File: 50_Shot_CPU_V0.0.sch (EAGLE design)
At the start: 74 parts, among them IC1 PIC24FJ128GA010, J1 J12, J10 22-23-2021, J11 22-23-2061, J12 A311422_nd, J13 22-23-2021, J14 22-23-2021, J2 J2, J3 22-23-2021, J4 22-23-2021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

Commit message: testing push/pull
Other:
- note added: "Adding this text, pushing, deleting from laptop, pulling"
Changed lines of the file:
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@@
 <?xml version="1.0" encoding="utf-8"?>
 <!DOCTYPE eagle SYSTEM "eagle.dtd">
-<eagle version="7.6.0">
+<eagle version="7.7.0">
 <drawing>
 <settings>
@@
 <frame x1="-182.88" y1="-76.2" x2="276.86" y2="220.98" columns="8" rows="5" layer="91"/>
 <text x="-129.54" y="-38.1" size="1.778" layer="91">***Note: Change R9 to 000 ohm if used for -X of touch screen. </text>
+<text x="132.08" y="167.64" size="1.778" layer="91">Adding this text, pushing, deleting from laptop, pulling</text>
 </plain>
 <instances>

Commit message: trying this again
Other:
- note added: "it worked, try yhis again"
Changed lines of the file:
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@@
 <text x="-129.54" y="-38.1" size="1.778" layer="91">***Note: Change R9 to 000 ohm if used for -X of touch screen. </text>
 <text x="132.08" y="167.64" size="1.778" layer="91">Adding this text, pushing, deleting from laptop, pulling</text>
+<text x="144.78" y="162.56" size="1.778" layer="91">it worked, try yhis again</text>
 </plain>
 <instances>

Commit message: add relay board
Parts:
- removed X4: 22-23-2111, con-molex:22-23-2111
- added R19: 1k, rcl-2:R-US_M0805
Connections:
- removed net RF3: IC1.U1TX/RF3, J11-1.S
- new net ###: J11-1.S
- new net SHIFT_EN: IC1.U1TX/RF3, R19.1, X5-7.S
- net +12V: now also C8.1, J1-4.S, X5-1.S
- net ARM_RELAY: no longer X5-7.S
- net VCC: no longer J1-4.S
- net VDD: now also R19.2; no longer C8.1, X5-1.S
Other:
- note removed: "Dummy Header"
- moved on the sheet: C17
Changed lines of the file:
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@@
 <part name="J14" library="Mine" deviceset="22-23-2021" device=""/>
 <part name="X5" library="con-molex" deviceset="22-23-2111" device=""/>
-<part name="X4" library="con-molex" deviceset="22-23-2111" device=""/>
 <part name="X3" library="con-molex" deviceset="22-23-2081" device=""/>
 <part name="C7" library="rcl" deviceset="C-US" device="C0805" value="0.01uF"/>
@@
 <part name="C23" library="Mine" deviceset="CAP3X3" device="" value="10uF"/>
 <part name="R18" library="rcl" deviceset="R-US_" device="M0805" value="1k"/>
+<part name="R19" library="rcl-2" deviceset="R-US_" device="M0805" value="1k"/>
 </parts>
 <sheets>
@@
 <text x="-22.86" y="86.36" size="1.778" layer="91">Circuit Board Header</text>
 <text x="-43.18" y="200.66" size="1.778" layer="91">I2C Header</text>
-<text x="-15.24" y="38.1" size="1.778" layer="91">Dummy Header</text>
 <text x="-142.24" y="152.4" size="1.778" layer="91">S/M Switch</text>
 <text x="-144.78" y="109.22" size="1.778" layer="91">Fire Switch</text>
@@
 <attribute name="VALUE" x="227.584" y="37.211" size="1.778" layer="96" rot="R180"/>
 </instance>
-<instance part="C17" gate="G$1" x="154.94" y="-40.64" smashed="yes" rot="R180">
-<attribute name="NAME" x="153.924" y="-41.275" size="1.778" layer="95" rot="R180"/>
-<attribute name="VALUE" x="153.924" y="-36.449" size="1.778" layer="96" rot="R180"/>
+<instance part="C17" gate="G$1" x="160.02" y="-40.64" smashed="yes" rot="R180">
+<attribute name="NAME" x="159.004" y="-41.275" size="1.778" layer="95" rot="R180"/>
+<attribute name="VALUE" x="159.004" y="-36.449" size="1.778" layer="96" rot="R180"/>
 </instance>
 <instance part="J13" gate="-1" x="2.54" y="149.86" smashed="yes" rot="R180">
@@
 <instance part="X5" gate="-10" x="-5.08" y="48.26"/>
 <instance part="X5" gate="-11" x="-5.08" y="45.72"/>
-<instance part="X4" gate="-1" x="-12.7" y="33.02"/>
-<instance part="X4" gate="-2" x="-12.7" y="30.48"/>
-<instance part="X4" gate="-3" x="-12.7" y="27.94"/>
-<instance part="X4" gate="-4" x="-12.7" y="25.4"/>
-<instance part="X4" gate="-5" x="-12.7" y="22.86"/>
-<instance part="X4" gate="-6" x="-12.7" y="20.32"/>
-<instance part="X4" gate="-7" x="-12.7" y="17.78"/>
-<instance part="X4" gate="-8" x="-12.7" y="15.24"/>
-<instance part="X4" gate="-9" x="-12.7" y="12.7"/>
-<instance part="X4" gate="-10" x="-12.7" y="10.16"/>
-<instance part="X4" gate="-11" x="-12.7" y="7.62"/>
 <instance part="X3" gate="-1" x="-33.02" y="180.34" rot="R180"/>
 <instance part="X3" gate="-2" x="-33.02" y="182.88" rot="R180"/>
@@
 <attribute name="NAME" x="-135.128" y="130.0734" size="1.778" layer="95" rot="R180"/>
 <attribute name="VALUE" x="-124.714" y="125.73" size="1.778" layer="96" rot="R180"/>
+</instance>
+<instance part="R19" gate="G$1" x="203.2" y="-25.4" smashed="yes" rot="R90">
+<attribute name="NAME" x="201.7014" y="-29.21" size="1.778" layer="95" rot="R90"/>
+<attribute name="VALUE" x="206.502" y="-29.21" size="1.778" layer="96" rot="R90"/>
 </instance>
 </instances>
@@
 <wire x1="5.08" y1="149.86" x2="15.24" y2="149.86" width="0.1524" layer="91"/>
 </segment>
+<segment>
+<wire x1="-7.62" y1="71.12" x2="-15.24" y2="71.12" width="0.1524" layer="91"/>
+<label x="-15.24" y="71.12" size="1.778" layer="95" rot="R180" xref="yes"/>
+<pinref part="C8" gate="G$1" pin="1"/>
+<wire x1="-12.7" y1="81.28" x2="-12.7" y2="83.82" width="0.1524" layer="91"/>
+<wire x1="-12.7" y1="83.82" x2="-7.62" y2="83.82" width="0.1524" layer="91"/>
+<wire x1="-7.62" y1="83.82" x2="-7.62" y2="71.12" width="0.1524" layer="91"/>
+<pinref part="X5" gate="-1" pin="S"/>
+<junction x="-7.62" y="71.12"/>
+</segment>
+<segment>
+<pinref part="J1" gate="-4" pin="S"/>
+<wire x1="-157.48" y1="132.08" x2="-111.76" y2="132.08" width="0.1524" layer="91"/>
+<label x="-111.76" y="132.08" size="1.778" layer="95" xref="yes"/>
+</segment>
 </net>
 <net name="GND" class="0">
@@
 <junction x="15.24" y="-2.54"/>
 <junction x="15.24" y="-35.56"/>
-<wire x1="154.94" y1="-35.56" x2="147.32" y2="-35.56" width="0.1524" layer="91"/>
+<wire x1="160.02" y1="-35.56" x2="147.32" y2="-35.56" width="0.1524" layer="91"/>
 <wire x1="147.32" y1="-35.56" x2="124.46" y2="-35.56" width="0.1524" layer="91"/>
 <wire x1="124.46" y1="-35.56" x2="111.76" y2="-35.56" width="0.1524" layer="91"/>
@@
 <label x="261.62" y="127" size="1.778" layer="95" xref="yes"/>
 </segment>
-<segment>
-<pinref part="J1" gate="-4" pin="S"/>
-<wire x1="-157.48" y1="132.08" x2="-111.76" y2="132.08" width="0.1524" layer="91"/>
-<label x="-111.76" y="132.08" size="1.778" layer="95" xref="yes"/>
-</segment>
 </net>
 <net name="VDD" class="0">
@@
 <wire x1="60.96" y1="48.26" x2="27.94" y2="48.26" width="0.1524" layer="91"/>
 <junction x="27.94" y="48.26"/>
-<wire x1="27.94" y1="93.98" x2="231.14" y2="93.98" width="0.1524" layer="91"/>
+<wire x1="27.94" y1="93.98" x2="238.76" y2="93.98" width="0.1524" layer="91"/>
 <junction x="27.94" y="93.98"/>
-<wire x1="231.14" y1="93.98" x2="231.14" y2="17.78" width="0.1524" layer="91"/>
+<wire x1="238.76" y1="93.98" x2="238.76" y2="17.78" width="0.1524" layer="91"/>
 <pinref part="IC1" gate="G$1" pin="VDD@5"/>
 <pinref part="IC1" gate="G$1" pin="VDD@4"/>
-<wire x1="231.14" y1="17.78" x2="223.52" y2="17.78" width="0.1524" layer="91"/>
+<wire x1="238.76" y1="17.78" x2="223.52" y2="17.78" width="0.1524" layer="91"/>
 <wire x1="223.52" y1="17.78" x2="195.58" y2="17.78" width="0.1524" layer="91"/>
 <wire x1="149.86" y1="-17.78" x2="149.86" y2="-45.72" width="0.1524" layer="91"/>
-<wire x1="149.86" y1="-45.72" x2="154.94" y2="-45.72" width="0.1524" layer="91"/>
-<wire x1="154.94" y1="-45.72" x2="231.14" y2="-45.72" width="0.1524" layer="91"/>
-<wire x1="231.14" y1="-45.72" x2="231.14" y2="17.78" width="0.1524" layer="91"/>
-<junction x="231.14" y="17.78"/>
+<wire x1="149.86" y1="-45.72" x2="160.02" y2="-45.72" width="0.1524" layer="91"/>
+<wire x1="160.02" y1="-45.72" x2="238.76" y2="-45.72" width="0.1524" layer="91"/>
+<wire x1="238.76" y1="-45.72" x2="238.76" y2="17.78" width="0.1524" layer="91"/>
+<junction x="238.76" y="17.78"/>
 <pinref part="C11" gate="G$1" pin="1"/>
 <wire x1="22.86" y1="38.1" x2="22.86" y2="48.26" width="0.1524" layer="91"/>
@@
 <wire x1="127" y1="-45.72" x2="149.86" y2="-45.72" width="0.1524" layer="91"/>
 <pinref part="C17" gate="G$1" pin="1"/>
-<wire x1="154.94" y1="-43.18" x2="154.94" y2="-45.72" width="0.1524" layer="91"/>
-<junction x="154.94" y="-45.72"/>
+<wire x1="160.02" y1="-43.18" x2="160.02" y2="-45.72" width="0.1524" layer="91"/>
+<junction x="160.02" y="-45.72"/>
 <pinref part="IC1" gate="G$1" pin="VDD@3"/>
 <wire x1="127" y1="-17.78" x2="127" y2="-45.72" width="0.1524" layer="91"/>
@@
 </segment>
 <segment>
-<wire x1="-7.62" y1="71.12" x2="-17.78" y2="71.12" width="0.1524" layer="91"/>
-<label x="-17.78" y="71.12" size="1.778" layer="95" rot="R180" xref="yes"/>
-<pinref part="C8" gate="G$1" pin="1"/>
-<wire x1="-12.7" y1="81.28" x2="-12.7" y2="83.82" width="0.1524" layer="91"/>
-<wire x1="-12.7" y1="83.82" x2="-7.62" y2="83.82" width="0.1524" layer="91"/>
-<wire x1="-7.62" y1="83.82" x2="-7.62" y2="71.12" width="0.1524" layer="91"/>
-<pinref part="X5" gate="-1" pin="S"/>
-<junction x="-7.62" y="71.12"/>
-</segment>
-<segment>
 <pinref part="X3" gate="-8" pin="S"/>
 <label x="-17.78" y="198.12" size="1.778" layer="95" xref="yes"/>
@@
 <wire x1="58.42" y1="5.08" x2="55.88" y2="5.08" width="0.1524" layer="91"/>
 <label x="55.88" y="5.08" size="1.778" layer="95" rot="R180" xref="yes"/>
+</segment>
+<segment>
+<pinref part="R19" gate="G$1" pin="2"/>
+<wire x1="203.2" y1="-20.32" x2="203.2" y2="-17.78" width="0.1524" layer="91"/>
+<wire x1="203.2" y1="-17.78" x2="205.74" y2="-17.78" width="0.1524" layer="91"/>
+<label x="205.74" y="-17.78" size="1.778" layer="95" xref="yes"/>
 </segment>
 </net>
@@
 </segment>
 </net>
-<net name="RF3" class="0">
-<segment>
-<pinref part="IC1" gate="G$1" pin="U1TX/RF3"/>
-<wire x1="195.58" y1="-10.16" x2="198.12" y2="-10.16" width="0.1524" layer="91"/>
-<wire x1="198.12" y1="-10.16" x2="198.12" y2="-17.78" width="0.1524" layer="91"/>
-<wire x1="198.12" y1="-17.78" x2="203.2" y2="-17.78" width="0.1524" layer="91"/>
-<label x="203.2" y="-17.78" size="1.778" layer="95" xref="yes"/>
-</segment>
+<net name="###" class="0">
 <segment>
 <wire x1="-48.26" y1="7.62" x2="-33.02" y2="7.62" width="0.1524" layer="91"/>
@@
 <wire x1="-101.6" y1="144.78" x2="-111.76" y2="144.78" width="0.1524" layer="91"/>
 <label x="-111.76" y="144.78" size="1.778" layer="95" rot="R180" xref="yes"/>
-</segment>
-<segment>
-<wire x1="-7.62" y1="55.88" x2="-10.16" y2="55.88" width="0.1524" layer="91"/>
-<label x="-10.16" y="55.88" size="1.778" layer="95" rot="R180" xref="yes"/>
-<pinref part="X5" gate="-7" pin="S"/>
 </segment>
 </net>
@@
 </segment>
 </net>
+<net name="SHIFT_EN" class="0">
+<segment>
+<wire x1="-7.62" y1="55.88" x2="-10.16" y2="55.88" width="0.1524" layer="91"/>
+<label x="-10.16" y="55.88" size="1.778" layer="95" rot="R180" xref="yes"/>
+<pinref part="X5" gate="-7" pin="S"/>
+</segment>
+<segment>
+<pinref part="IC1" gate="G$1" pin="U1TX/RF3"/>
+<wire x1="195.58" y1="-10.16" x2="198.12" y2="-10.16" width="0.1524" layer="91"/>
+<wire x1="198.12" y1="-10.16" x2="198.12" y2="-33.02" width="0.1524" layer="91"/>
+<wire x1="198.12" y1="-33.02" x2="203.2" y2="-33.02" width="0.1524" layer="91"/>
+<label x="210.82" y="-33.02" size="1.778" layer="95" xref="yes"/>
+<pinref part="R19" gate="G$1" pin="1"/>
+<wire x1="203.2" y1="-33.02" x2="210.82" y2="-33.02" width="0.1524" layer="91"/>
+<wire x1="203.2" y1="-30.48" x2="203.2" y2="-33.02" width="0.1524" layer="91"/>
+<junction x="203.2" y="-33.02"/>
+</segment>
+</net>

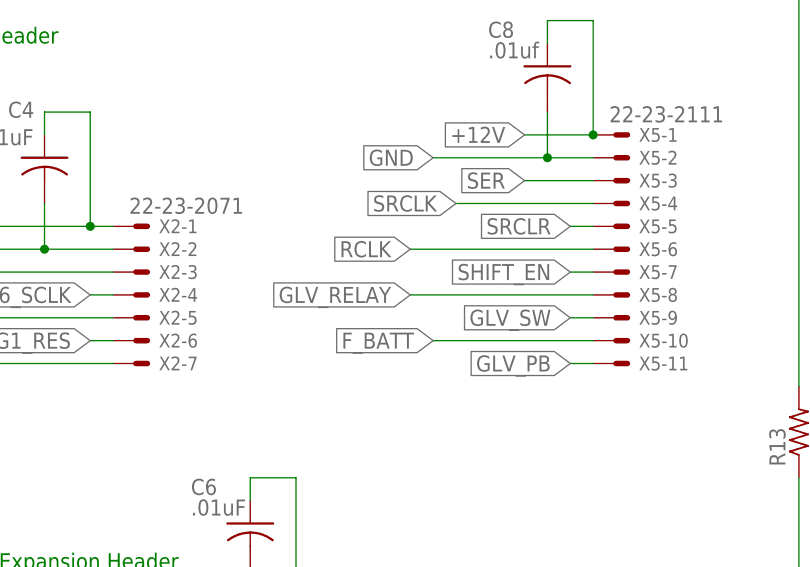
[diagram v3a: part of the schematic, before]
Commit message: add proper relay board
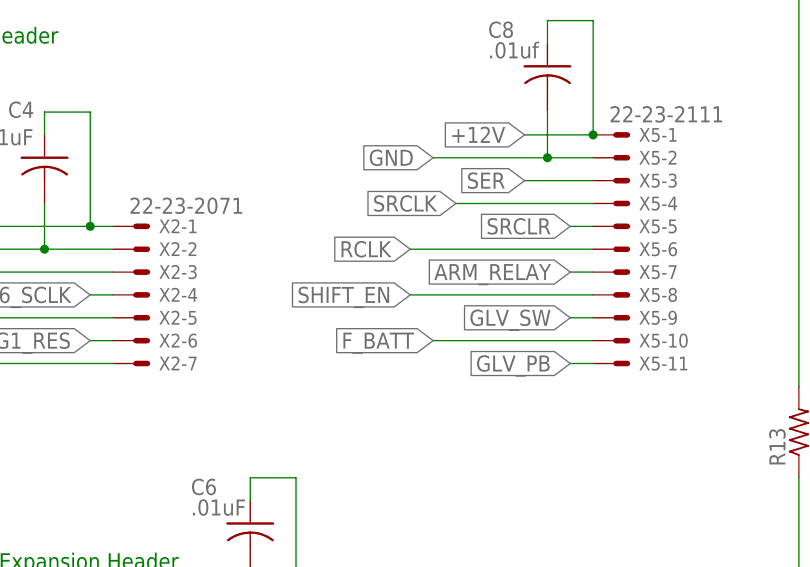
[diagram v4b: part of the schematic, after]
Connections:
- net ARM_RELAY: now also X5-7.S
- net GLV_RELAY: no longer X5-8.S
- net SHIFT_EN: now also X5-8.S; no longer X5-7.S
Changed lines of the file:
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@@
 <net name="GLV_RELAY" class="0">
-<segment>
-<wire x1="-7.62" y1="53.34" x2="-27.94" y2="53.34" width="0.1524" layer="91"/>
-<label x="-27.94" y="53.34" size="1.778" layer="95" rot="R180" xref="yes"/>
-<pinref part="X5" gate="-8" pin="S"/>
-</segment>
 <segment>
 <label x="43.18" y="210.82" size="1.778" layer="95" rot="R180" xref="yes"/>
@@
 <wire x1="-101.6" y1="144.78" x2="-111.76" y2="144.78" width="0.1524" layer="91"/>
 <label x="-111.76" y="144.78" size="1.778" layer="95" rot="R180" xref="yes"/>
+</segment>
+<segment>
+<wire x1="-7.62" y1="55.88" x2="-10.16" y2="55.88" width="0.1524" layer="91"/>
+<label x="-10.16" y="55.88" size="1.778" layer="95" rot="R180" xref="yes"/>
+<pinref part="X5" gate="-7" pin="S"/>
 </segment>
 </net>
@@
 <net name="SHIFT_EN" class="0">
 <segment>
-<wire x1="-7.62" y1="55.88" x2="-10.16" y2="55.88" width="0.1524" layer="91"/>
-<label x="-10.16" y="55.88" size="1.778" layer="95" rot="R180" xref="yes"/>
-<pinref part="X5" gate="-7" pin="S"/>
-</segment>
-<segment>
 <pinref part="IC1" gate="G$1" pin="U1TX/RF3"/>
 <wire x1="195.58" y1="-10.16" x2="198.12" y2="-10.16" width="0.1524" layer="91"/>
@@
 <junction x="203.2" y="-33.02"/>
 </segment>
-</net>
+<segment>
+<wire x1="-7.62" y1="53.34" x2="-27.94" y2="53.34" width="0.1524" layer="91"/>
+<label x="-27.94" y="53.34" size="1.778" layer="95" rot="R180" xref="yes"/>
+<pinref part="X5" gate="-8" pin="S"/>
+</segment>
+</net>
